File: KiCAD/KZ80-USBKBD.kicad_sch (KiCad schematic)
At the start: 34 parts, among them J1 SBC8080 BUS, J2 CON-A, J3 CMT-OUT, J4 232C(DEBUG), J5 ADR-JP2, J6 ADR-JP1, SW1 SW_SPST, U1 Pico, U2 8255, U3 74HC139, U4 74HC00

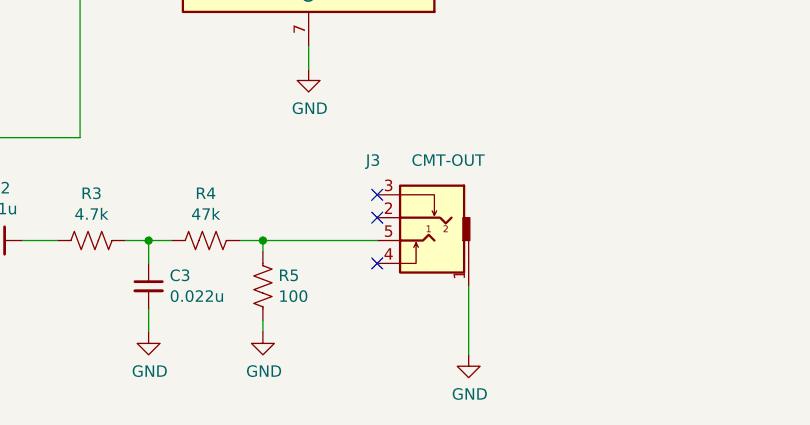
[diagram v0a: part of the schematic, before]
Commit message: REV2 基板 回路不足部分追加・パターン修正・ガーバー再出力
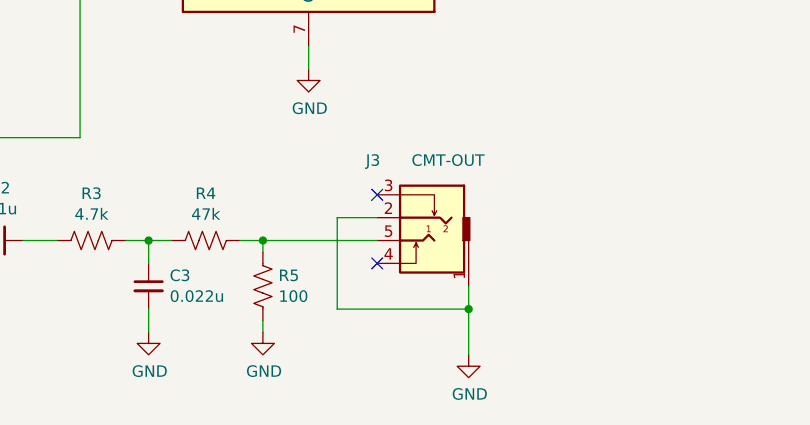
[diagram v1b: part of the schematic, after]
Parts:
- U3: footprint Package_DIP:DIP-16_W7.62mm_LongPads -> (none)
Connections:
- net GND: now also J3.2
- no-connect marks 42 -> 41
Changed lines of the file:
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@@
   (junction (at 132.08 173.99) (diameter 0) (color 0 0 0 0)
+  )
+  (junction (at 167.64 181.61) (diameter 0) (color 0 0 0 0)
   )
   (junction (at 49.53 24.13) (diameter 0) (color 0 0 0 0)
@@
   (no_connect (at 39.37 140.97))
   (no_connect (at 74.93 107.95))
-  (no_connect (at 157.48 171.45))
   (no_connect (at 74.93 110.49))
   (no_connect (at 39.37 128.27))
@@
     (stroke (width 0) (type default) (color 0 0 0 0))
   )
+  (wire (pts (xy 153.035 171.45) (xy 153.035 181.61))
+    (stroke (width 0) (type default) (color 0 0 0 0))
+  )
   (wire (pts (xy 29.21 21.59) (xy 29.21 24.13))
     (stroke (width 0) (type default) (color 0 0 0 0))
@@
     (stroke (width 0) (type default) (color 0 0 0 0))
   )
+  (wire (pts (xy 153.035 181.61) (xy 167.64 181.61))
+    (stroke (width 0) (type default) (color 0 0 0 0))
+  )
   (wire (pts (xy 33.02 130.81) (xy 39.37 130.81))
     (stroke (width 0) (type default) (color 0 0 0 0))
@@
     (stroke (width 0) (type default) (color 0 0 0 0))
   )
+  (wire (pts (xy 157.48 171.45) (xy 153.035 171.45))
+    (stroke (width 0) (type default) (color 0 0 0 0))
+  )
   (wire (pts (xy 236.22 80.01) (xy 241.3 80.01))
     (stroke (width 0) (type default) (color 0 0 0 0))
@@
     (stroke (width 0) (type default) (color 0 0 0 0))
   )
-  (wire (pts (xy 167.64 179.07) (xy 167.64 186.69))
+  (wire (pts (xy 167.64 179.07) (xy 167.64 181.61))
     (stroke (width 0) (type default) (color 0 0 0 0))
   )
@@
   )
   (wire (pts (xy 74.93 130.81) (xy 81.28 130.81))
+    (stroke (width 0) (type default) (color 0 0 0 0))
+  )
+  (wire (pts (xy 167.64 181.61) (xy 167.64 186.69))
     (stroke (width 0) (type default) (color 0 0 0 0))
   )
@@
     (property "Reference" "U3" (id 0) (at 208.28 62.23 0))
     (property "Value" "74HC139" (id 1) (at 208.28 69.85 0))
-    (property "Footprint" "Package_DIP:DIP-16_W7.62mm_LongPads" (id 2) (at 208.28 60.96 0)
+    (property "Footprint" "" (id 2) (at 208.28 60.96 0)
       (effects (font (size 1.27 1.27)) hide)
     )
@@
     (pin "6")
     (pin "7")
-  )
-  (symbol (lib_id "74xx:74LS139") (at 208.28 80.01 0) (unit 2)
-    (in_bom yes) (on_board yes)
-    (property "Reference" "U3" (id 0) (at 208.28 81.28 0))
-    (property "Value" "74HC139" (id 1) (at 208.28 88.9 0))
-    (property "Footprint" "Package_DIP:DIP-16_W7.62mm_LongPads" (id 2) (at 208.28 80.01 0)
-      (effects (font (size 1.27 1.27)) hide)
-    )
-    (property "Datasheet" "http://www.ti.com/lit/gpn/sn74LS139" (id 3) (at 208.28 80.01 0)
-      (effects (font (size 1.27 1.27)) hide)
-    )
     (pin "10")
     (pin "11")
@@
     (pin "15")
     (pin "9")
+    (pin "16")
+    (pin "8")
+  )
+  (symbol (lib_id "74xx:74LS139") (at 208.28 80.01 0) (unit 2)
+    (in_bom yes) (on_board yes)
+    (property "Reference" "U3" (id 0) (at 208.28 81.28 0))
+    (property "Value" "74HC139" (id 1) (at 208.28 88.9 0))
+    (property "Footprint" "" (id 2) (at 208.28 80.01 0)
+      (effects (font (size 1.27 1.27)) hide)
+    )
+    (property "Datasheet" "http://www.ti.com/lit/gpn/sn74LS139" (id 3) (at 208.28 80.01 0)
+      (effects (font (size 1.27 1.27)) hide)
+    )
+    (pin "1")
+    (pin "2")
+    (pin "3")
+    (pin "4")
+    (pin "5")
+    (pin "6")
+    (pin "7")
+    (pin "10")
+    (pin "11")
+    (pin "12")
+    (pin "13")
+    (pin "14")
+    (pin "15")
+    (pin "9")
+    (pin "16")
+    (pin "8")
   )
   (symbol (lib_id "74xx:74LS139") (at 208.28 133.35 0) (unit 3)
@@
       (effects (font (size 1.27 1.27)) (justify left))
     )
-    (property "Footprint" "Package_DIP:DIP-16_W7.62mm_LongPads" (id 2) (at 208.28 133.35 0)
+    (property "Footprint" "" (id 2) (at 208.28 133.35 0)
       (effects (font (size 1.27 1.27)) hide)
     )
@@
       (effects (font (size 1.27 1.27)) hide)
     )
+    (pin "1")
+    (pin "2")
+    (pin "3")
+    (pin "4")
+    (pin "5")
+    (pin "6")
+    (pin "7")
+    (pin "10")
+    (pin "11")
+    (pin "12")
+    (pin "13")
+    (pin "14")
+    (pin "15")
+    (pin "9")
     (pin "16")
     (pin "8")
@@
       (effects (font (size 1.27 1.27)) hide)
     )
+    (pin "1")
+    (pin "2")
+    (pin "3")
+    (pin "4")
+    (pin "5")
+    (pin "6")
+    (pin "10")
+    (pin "8")
+    (pin "9")
+    (pin "11")
+    (pin "12")
+    (pin "13")
     (pin "14")
     (pin "7")
@@
       (effects (font (size 1.27 1.27)) hide)
     )
+    (pin "1")
+    (pin "2")
+    (pin "3")
+    (pin "4")
+    (pin "5")
+    (pin "6")
     (pin "10")
     (pin "8")
     (pin "9")
+    (pin "11")
+    (pin "12")
+    (pin "13")
+    (pin "14")
+    (pin "7")
   )
   (symbol (lib_id "Connector_Generic:Conn_01x06") (at 170.18 27.94 0) (unit 1)
@@
     )
     (path "/00000000-0000-0000-0000-00005d5b4e95"
-      (reference "U3") (unit 1) (value "74HC139") (footprint "Package_DIP:DIP-16_W7.62mm_LongPads")
+      (reference "U3") (unit 1) (value "74HC139") (footprint "Package_DIP:DIP-16_W7.62mm_Socket")
     )
     (path "/00000000-0000-0000-0000-00005d5b4ed2"
-      (reference "U3") (unit 2) (value "74HC139") (footprint "Package_DIP:DIP-16_W7.62mm_LongPads")
+      (reference "U3") (unit 2) (value "74HC139") (footprint "Package_DIP:DIP-16_W7.62mm_Socket")
     )
     (path "/00000000-0000-0000-0000-00005d5b5011"
-      (reference "U3") (unit 3) (value "74HC139") (footprint "Package_DIP:DIP-16_W7.62mm_LongPads")
+      (reference "U3") (unit 3) (value "74HC139") (footprint "Package_DIP:DIP-16_W7.62mm_Socket")
     )
     (path "/00000000-0000-0000-0000-00005d69d228"
